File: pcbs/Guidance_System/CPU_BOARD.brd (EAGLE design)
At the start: 100 x 52.1 mm, 33 parts, among them J1 22-27-2081-08, J10 22-27-2081-08, J11 22-27-2081-08, J12 22-27-2081-08, J13 22-27-2081-08, J14 22-27-2081-08, J15 22-27-2041-04, J16 22-27-2041-04, J17 22-27-2021-02, J2 22-27-2021-02, J3 22-27-2041-04, J4 22-27-2041-04, J5 22-27-2081-08, J6 22-27-2021-02, J7 22-27-2081-08, J8 22-27-2021-02, J9 22-27-2021-02

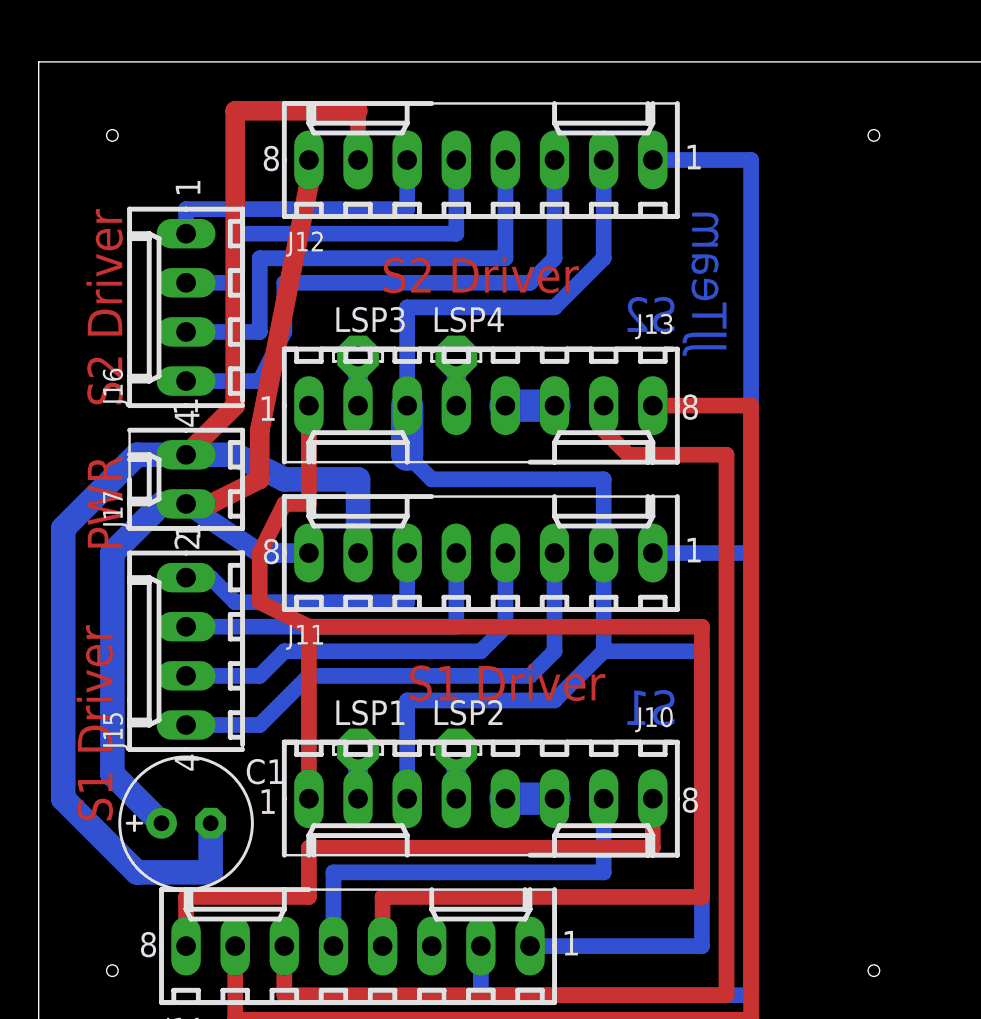
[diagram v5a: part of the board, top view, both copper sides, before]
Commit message: * Moved Capacitor to location where it will fit lying down * Moved JJTeam logo to place where it won't be drilled out.
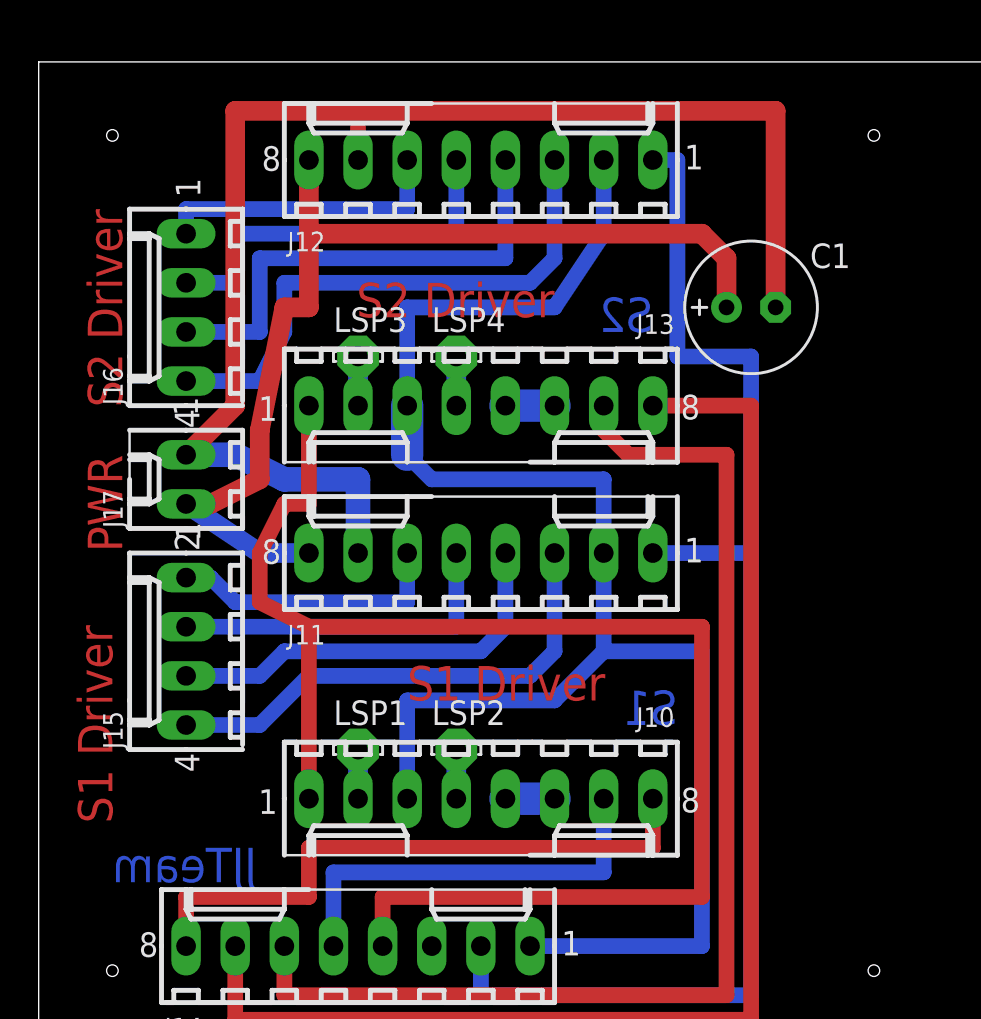
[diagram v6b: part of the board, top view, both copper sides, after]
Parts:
- moved C1 39.6 mm to (36.8, 64.8)
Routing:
- net N$31: track 47.9 -> 53.8 mm
- net N$34: track 74.4 -> 72.5 mm
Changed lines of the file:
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@@
 <wire x1="0" y1="77.46" x2="0" y2="25.4" width="0" layer="20"/>
 <text x="19.05" y="44.45" size="1.778" layer="1">S1 Driver</text>
-<text x="27.94" y="67.31" size="1.778" layer="1" rot="R180">S2 Driver</text>
+<text x="26.67" y="66.04" size="1.778" layer="1" rot="R180">S2 Driver</text>
 <hole x="3.81" y="30.48" drill="0.6"/>
 <hole x="57.15" y="30.48" drill="0.6"/>
@@
 <text x="95.25" y="71.12" size="1.778" layer="1" rot="R90">i2c</text>
 <text x="99.06" y="35.56" size="1.778" layer="1" rot="R90">Status</text>
-<text x="35.56" y="69.85" size="1.778" layer="16" rot="MR270">JJTeam</text>
+<text x="3.81" y="36.83" size="1.778" layer="16" rot="MR180">JJTeam</text>
 <text x="60.96" y="67.31" size="1.778" layer="16" rot="MR270">JJTeam</text>
 <text x="33.02" y="43.18" size="1.778" layer="16" rot="MR0">S1</text>
-<text x="33.02" y="63.5" size="1.778" layer="16" rot="MR0">S2</text>
+<text x="31.75" y="63.5" size="1.778" layer="16" rot="MR0">S2</text>
 <text x="76.2" y="76.2" size="1.778" layer="16" rot="MR180">gyro</text>
 <text x="87.63" y="41.91" size="1.778" layer="16" rot="MR90">fram</text>
@@
 <element name="R8" library="rcl" package="0204/5" value="" x="68.58" y="59.69" rot="R270"/>
 <element name="LSP5" library="solpad" package="LSP11" value="LSP11" x="77.47" y="68.58"/>
-<element name="C1" library="resistor" package="E2,5-7" value="" x="7.62" y="38.1"/>
+<element name="C1" library="resistor" package="E2,5-7" value="" x="36.83" y="64.77"/>
 </elements>
 <signals>
@@
 <contactref element="J10" pad="3"/>
 <contactref element="J13" pad="3"/>
-<wire x1="29.21" y1="72.39" x2="29.21" y2="67.31" width="0.8128" layer="16"/>
-<wire x1="29.21" y1="67.31" x2="26.67" y2="64.77" width="0.8128" layer="16"/>
+<wire x1="29.21" y1="72.39" x2="29.21" y2="68.58" width="0.8128" layer="16"/>
+<wire x1="29.21" y1="68.58" x2="26.67" y2="64.77" width="0.8128" layer="16"/>
 <wire x1="26.67" y1="64.77" x2="19.05" y2="64.77" width="0.8128" layer="16"/>
 <wire x1="19.05" y1="64.77" x2="19.05" y2="59.69" width="0.8128" layer="16"/>
@@
 <contactref element="J11" pad="1"/>
 <contactref element="J14" pad="2"/>
-<wire x1="31.75" y1="72.39" x2="36.83" y2="72.39" width="0.8128" layer="16"/>
-<wire x1="36.83" y1="72.39" x2="36.83" y2="52.07" width="0.8128" layer="16"/>
+<wire x1="31.75" y1="72.39" x2="33.02" y2="72.39" width="0.8128" layer="16"/>
+<wire x1="33.02" y1="72.39" x2="33.02" y2="62.23" width="0.8128" layer="16"/>
+<wire x1="33.02" y1="62.23" x2="36.83" y2="62.23" width="0.8128" layer="16"/>
+<wire x1="36.83" y1="62.23" x2="36.83" y2="52.07" width="0.8128" layer="16"/>
 <wire x1="31.75" y1="52.07" x2="36.83" y2="52.07" width="0.8128" layer="16"/>
 <wire x1="36.83" y1="52.07" x2="36.83" y2="29.21" width="0.8128" layer="16"/>
@@
 <wire x1="11.43" y1="52.07" x2="7.62" y2="54.61" width="1.016" layer="16"/>
 <wire x1="13.97" y1="72.39" x2="13.97" y2="71.12" width="1.016" layer="1"/>
-<wire x1="13.97" y1="71.12" x2="11.43" y2="58.42" width="1.016" layer="1"/>
+<wire x1="13.97" y1="68.58" x2="13.97" y2="64.77" width="1.016" layer="1"/>
+<wire x1="13.97" y1="64.77" x2="12.7" y2="64.77" width="1.016" layer="1"/>
+<wire x1="12.7" y1="64.77" x2="11.43" y2="58.42" width="1.016" layer="1"/>
 <wire x1="11.43" y1="58.42" x2="11.43" y2="55.88" width="1.016" layer="1"/>
 <wire x1="11.43" y1="55.88" x2="8.89" y2="54.61" width="1.016" layer="1"/>
 <wire x1="8.89" y1="54.61" x2="7.62" y2="54.61" width="1.016" layer="1"/>
 <contactref element="C1" pad="+"/>
-<wire x1="6.35" y1="38.1" x2="3.81" y2="40.64" width="1.27" layer="16"/>
-<wire x1="3.81" y1="40.64" x2="3.81" y2="52.07" width="1.27" layer="16"/>
-<wire x1="3.81" y1="52.07" x2="6.35" y2="54.61" width="1.27" layer="16"/>
-<wire x1="6.35" y1="54.61" x2="7.62" y2="54.61" width="1.27" layer="16"/>
+<wire x1="13.97" y1="71.12" x2="13.97" y2="68.58" width="1.016" layer="1"/>
+<wire x1="13.97" y1="68.58" x2="34.29" y2="68.58" width="1.016" layer="1"/>
+<wire x1="34.29" y1="68.58" x2="35.56" y2="67.31" width="1.016" layer="1"/>
+<wire x1="35.56" y1="67.31" x2="35.56" y2="64.77" width="1.016" layer="1"/>
 </signal>
 <signal name="N$34">
@@
 <wire x1="12.7" y1="55.88" x2="16.51" y2="55.88" width="1.27" layer="16"/>
 <wire x1="16.51" y1="55.88" x2="16.51" y2="52.07" width="1.27" layer="16"/>
-<wire x1="8.89" y1="38.1" x2="8.89" y2="35.56" width="1.27" layer="16"/>
-<wire x1="8.89" y1="35.56" x2="5.08" y2="35.56" width="1.27" layer="16"/>
-<wire x1="5.08" y1="35.56" x2="1.27" y2="39.37" width="1.27" layer="16"/>
-<wire x1="1.27" y1="39.37" x2="1.27" y2="53.34" width="1.27" layer="16"/>
-<wire x1="1.27" y1="53.34" x2="5.08" y2="57.15" width="1.27" layer="16"/>
-<wire x1="5.08" y1="57.15" x2="7.62" y2="57.15" width="1.27" layer="16"/>
+<wire x1="38.1" y1="64.77" x2="38.1" y2="74.93" width="1.016" layer="1"/>
+<wire x1="38.1" y1="74.93" x2="16.51" y2="74.93" width="1.016" layer="1"/>
 </signal>
 <signal name="N$35">

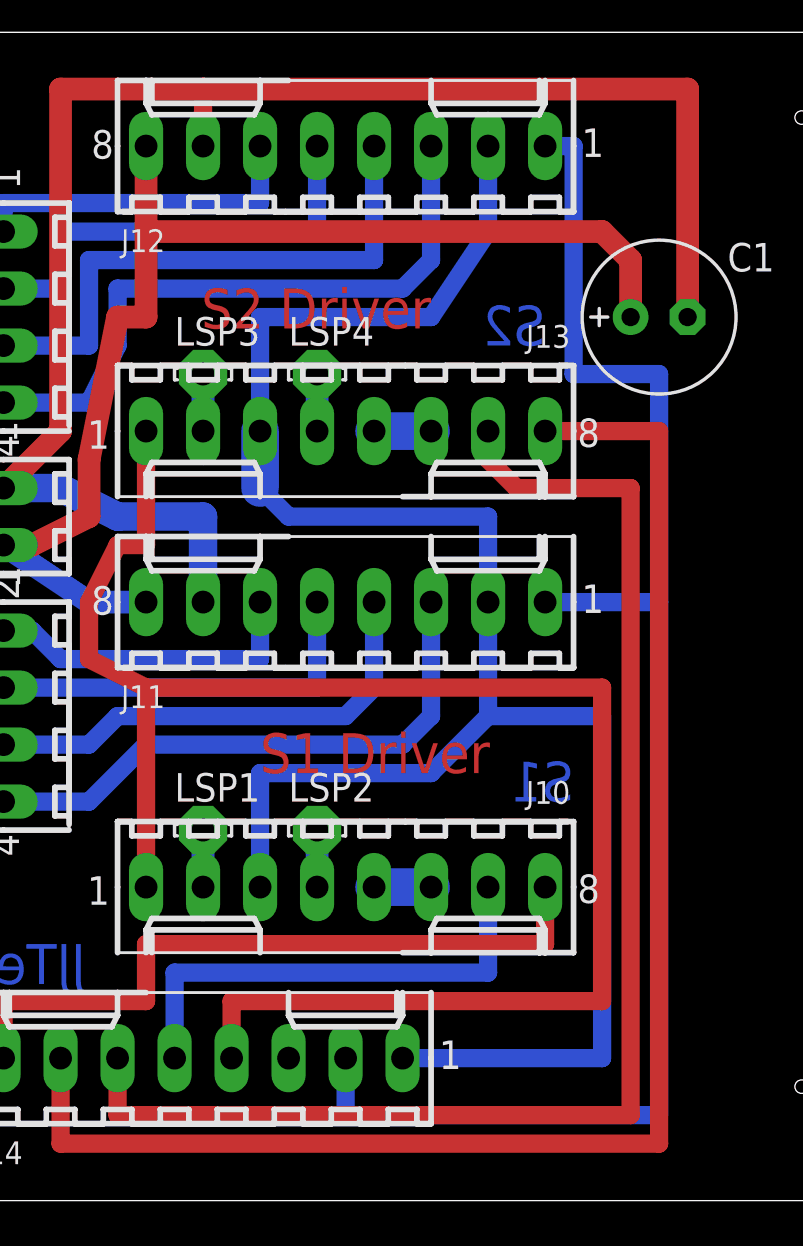
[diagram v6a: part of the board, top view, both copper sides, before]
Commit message: * Re-org of some tracks on driver side
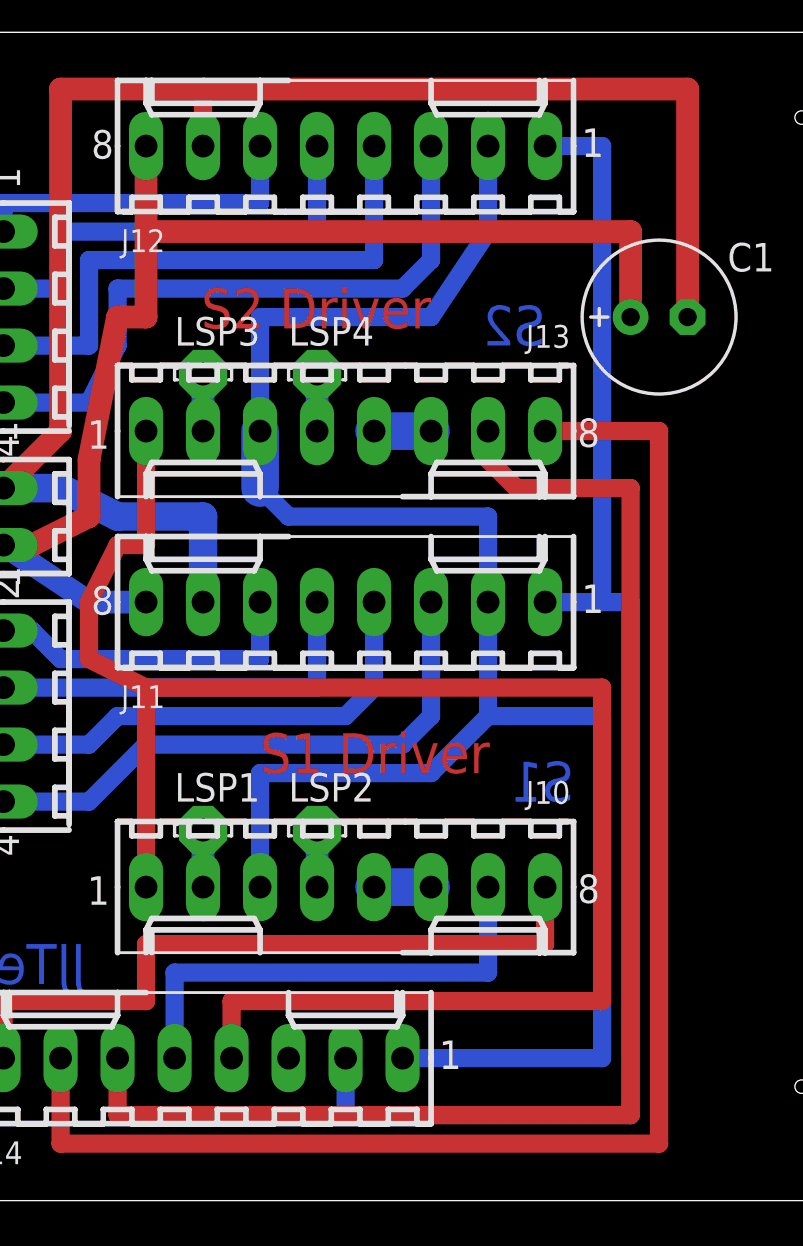
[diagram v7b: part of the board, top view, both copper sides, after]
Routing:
- net N$33: track 69.8 -> 64.8 mm
- net N$31: track 53.8 -> 54.5 mm
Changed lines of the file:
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@@
 <contactref element="J11" pad="1"/>
 <contactref element="J14" pad="2"/>
-<wire x1="31.75" y1="72.39" x2="33.02" y2="72.39" width="0.8128" layer="16"/>
-<wire x1="33.02" y1="72.39" x2="33.02" y2="62.23" width="0.8128" layer="16"/>
-<wire x1="33.02" y1="62.23" x2="36.83" y2="62.23" width="0.8128" layer="16"/>
-<wire x1="36.83" y1="62.23" x2="36.83" y2="52.07" width="0.8128" layer="16"/>
-<wire x1="31.75" y1="52.07" x2="36.83" y2="52.07" width="0.8128" layer="16"/>
-<wire x1="36.83" y1="52.07" x2="36.83" y2="29.21" width="0.8128" layer="16"/>
-<wire x1="36.83" y1="29.21" x2="22.86" y2="29.21" width="0.8128" layer="16"/>
+<wire x1="31.75" y1="72.39" x2="34.29" y2="72.39" width="0.8128" layer="16"/>
+<wire x1="34.29" y1="72.39" x2="34.29" y2="52.07" width="0.8128" layer="16"/>
+<wire x1="31.75" y1="52.07" x2="34.29" y2="52.07" width="0.8128" layer="16"/>
+<wire x1="34.29" y1="52.07" x2="35.56" y2="52.07" width="0.8128" layer="16"/>
+<wire x1="35.56" y1="52.07" x2="35.56" y2="29.21" width="0.8128" layer="16"/>
+<wire x1="35.56" y1="29.21" x2="22.86" y2="29.21" width="0.8128" layer="16"/>
 <wire x1="22.86" y1="29.21" x2="22.86" y2="31.75" width="0.8128" layer="16"/>
 </signal>
@@
 <wire x1="13.97" y1="52.07" x2="11.43" y2="52.07" width="1.016" layer="16"/>
 <wire x1="11.43" y1="52.07" x2="7.62" y2="54.61" width="1.016" layer="16"/>
-<wire x1="13.97" y1="72.39" x2="13.97" y2="71.12" width="1.016" layer="1"/>
 <wire x1="13.97" y1="68.58" x2="13.97" y2="64.77" width="1.016" layer="1"/>
 <wire x1="13.97" y1="64.77" x2="12.7" y2="64.77" width="1.016" layer="1"/>
@@
 <wire x1="8.89" y1="54.61" x2="7.62" y2="54.61" width="1.016" layer="1"/>
 <contactref element="C1" pad="+"/>
-<wire x1="13.97" y1="71.12" x2="13.97" y2="68.58" width="1.016" layer="1"/>
-<wire x1="13.97" y1="68.58" x2="34.29" y2="68.58" width="1.016" layer="1"/>
-<wire x1="34.29" y1="68.58" x2="35.56" y2="67.31" width="1.016" layer="1"/>
-<wire x1="35.56" y1="67.31" x2="35.56" y2="64.77" width="1.016" layer="1"/>
+<wire x1="13.97" y1="72.39" x2="13.97" y2="68.58" width="1.016" layer="1"/>
+<wire x1="13.97" y1="68.58" x2="35.56" y2="68.58" width="1.016" layer="1"/>
+<wire x1="35.56" y1="68.58" x2="35.56" y2="64.77" width="1.016" layer="1"/>
 </signal>
 <signal name="N$34">

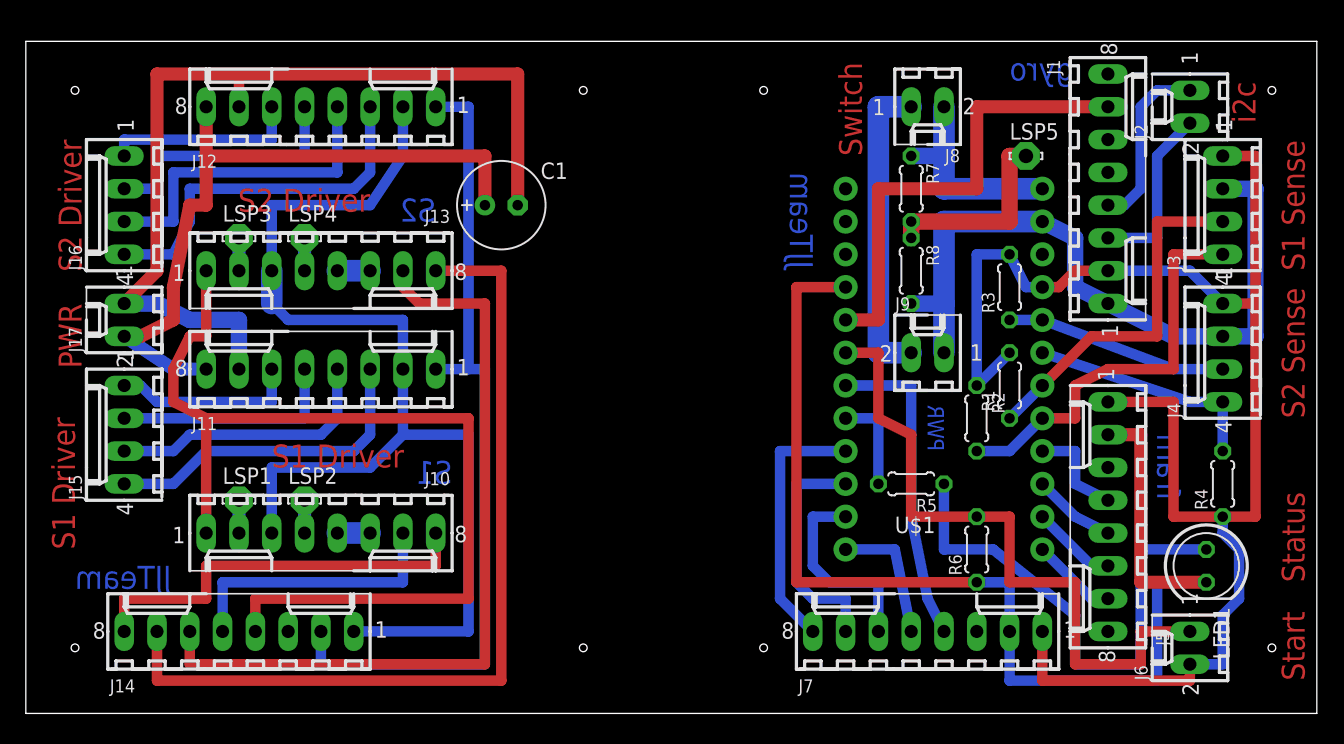
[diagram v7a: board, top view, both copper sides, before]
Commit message: * Moved 'start' top level track text to side...so it won't get drilled out.
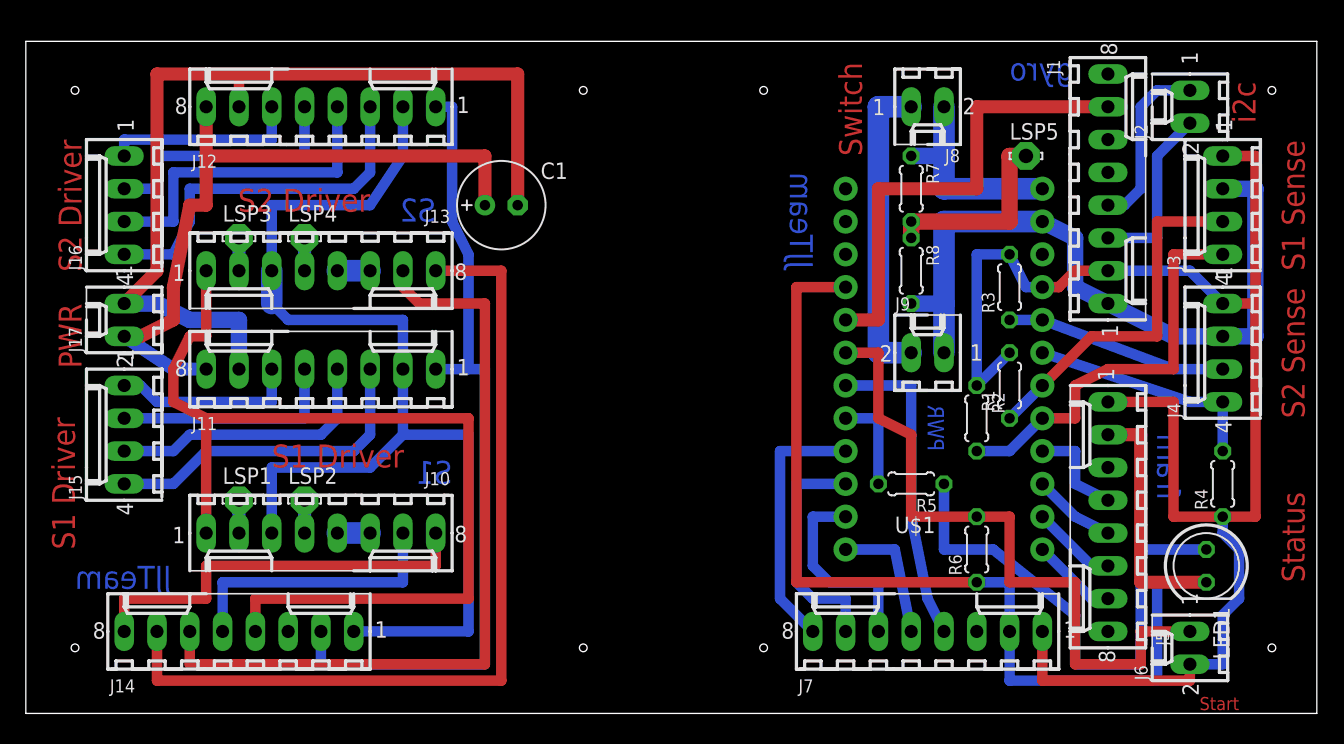
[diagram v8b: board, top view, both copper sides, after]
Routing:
- net N$33: track 64.8 -> 63.8 mm
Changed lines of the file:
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@@
 <text x="3.81" y="38.1" size="1.778" layer="1" rot="R90">S1 Driver</text>
 <text x="2.54" y="57.15" size="1.778" layer="1" rot="R270">PWR</text>
-<text x="99.06" y="27.94" size="1.778" layer="1" rot="R90">Start</text>
+<text x="93.98" y="26.67" size="1.016" layer="1" rot="R180">Start</text>
 <text x="99.06" y="59.69" size="1.778" layer="1" rot="R90">S1 Sense</text>
 <text x="99.06" y="48.26" size="1.778" layer="1" rot="R90">S2 Sense</text>
@@
 <contactref element="J11" pad="1"/>
 <contactref element="J14" pad="2"/>
-<wire x1="31.75" y1="72.39" x2="34.29" y2="72.39" width="0.8128" layer="16"/>
-<wire x1="34.29" y1="72.39" x2="34.29" y2="52.07" width="0.8128" layer="16"/>
+<wire x1="31.75" y1="72.39" x2="33.02" y2="72.39" width="0.8128" layer="16"/>
+<wire x1="33.02" y1="72.39" x2="33.02" y2="63.5" width="0.8128" layer="16"/>
+<wire x1="33.02" y1="63.5" x2="34.29" y2="60.96" width="0.8128" layer="16"/>
+<wire x1="34.29" y1="60.96" x2="34.29" y2="52.07" width="0.8128" layer="16"/>
 <wire x1="31.75" y1="52.07" x2="34.29" y2="52.07" width="0.8128" layer="16"/>
 <wire x1="34.29" y1="52.07" x2="35.56" y2="52.07" width="0.8128" layer="16"/>
